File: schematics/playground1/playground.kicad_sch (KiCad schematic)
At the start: 65 parts, among them J1 Conn_01x05, J2 Conn_02x03_Odd_Even, J3 Conn_01x03, J4 Conn_02x04_Odd_Even, SW1 SW_SPST, SW2 SW_Push, SW3 SW_Push, U1 ADS1299, U2 MCP1700x-330xxTT, U3 PIC32MX250F128B_I_SS, U5 LM2931AZ-5.0_TO92, Y1 8MHz

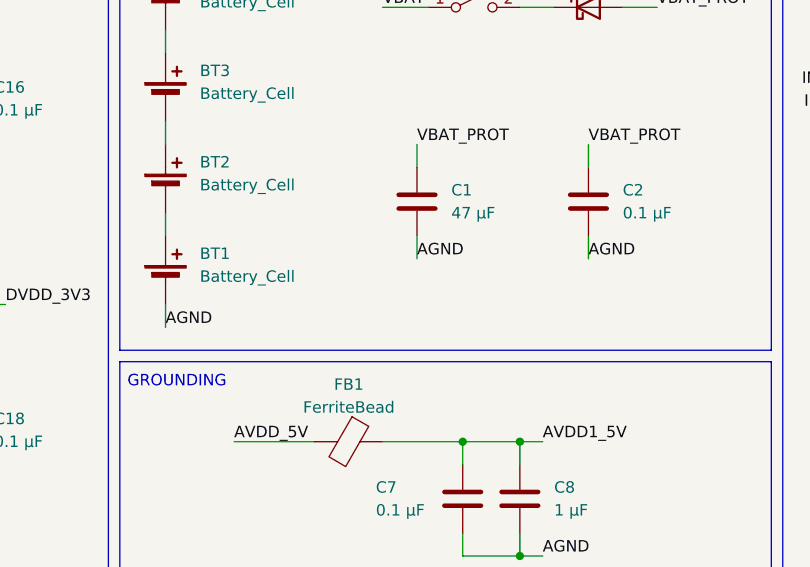
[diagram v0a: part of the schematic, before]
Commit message: change power subsystem to be dgnd, generate gerbers
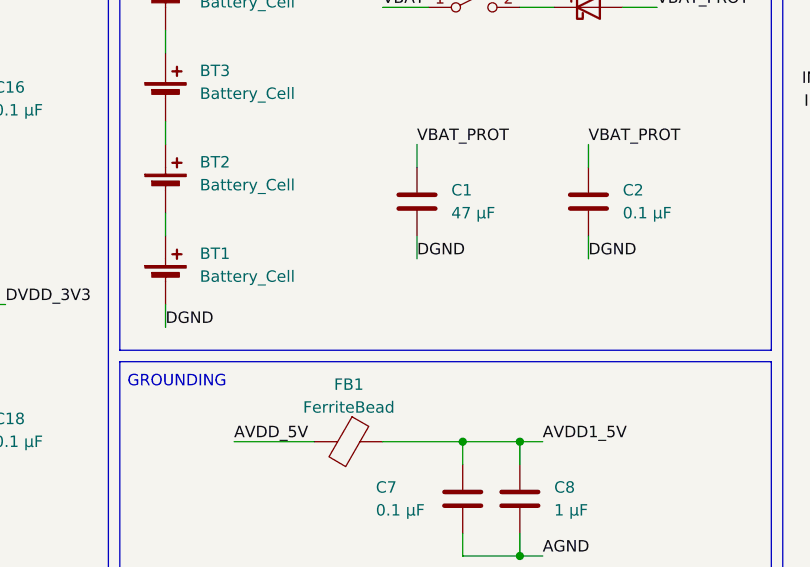
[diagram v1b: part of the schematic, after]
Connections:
- net AGND: no longer BT1.2 (-), C1.2, C2.2
- net DGND: now also BT1.2 (-), C1.2, C2.2
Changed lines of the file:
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@@
 		)
 	)
-	(label "AGND"
+	(label "DGND"
 		(at 196.85 91.44 0)
 		(effects
@@
 		)
 	)
-	(label "AGND"
+	(label "DGND"
 		(at 224.79 83.82 0)
 		(effects
@@
 		)
 	)
-	(label "AGND"
+	(label "DGND"
 		(at 243.84 83.82 0)
 		(effects

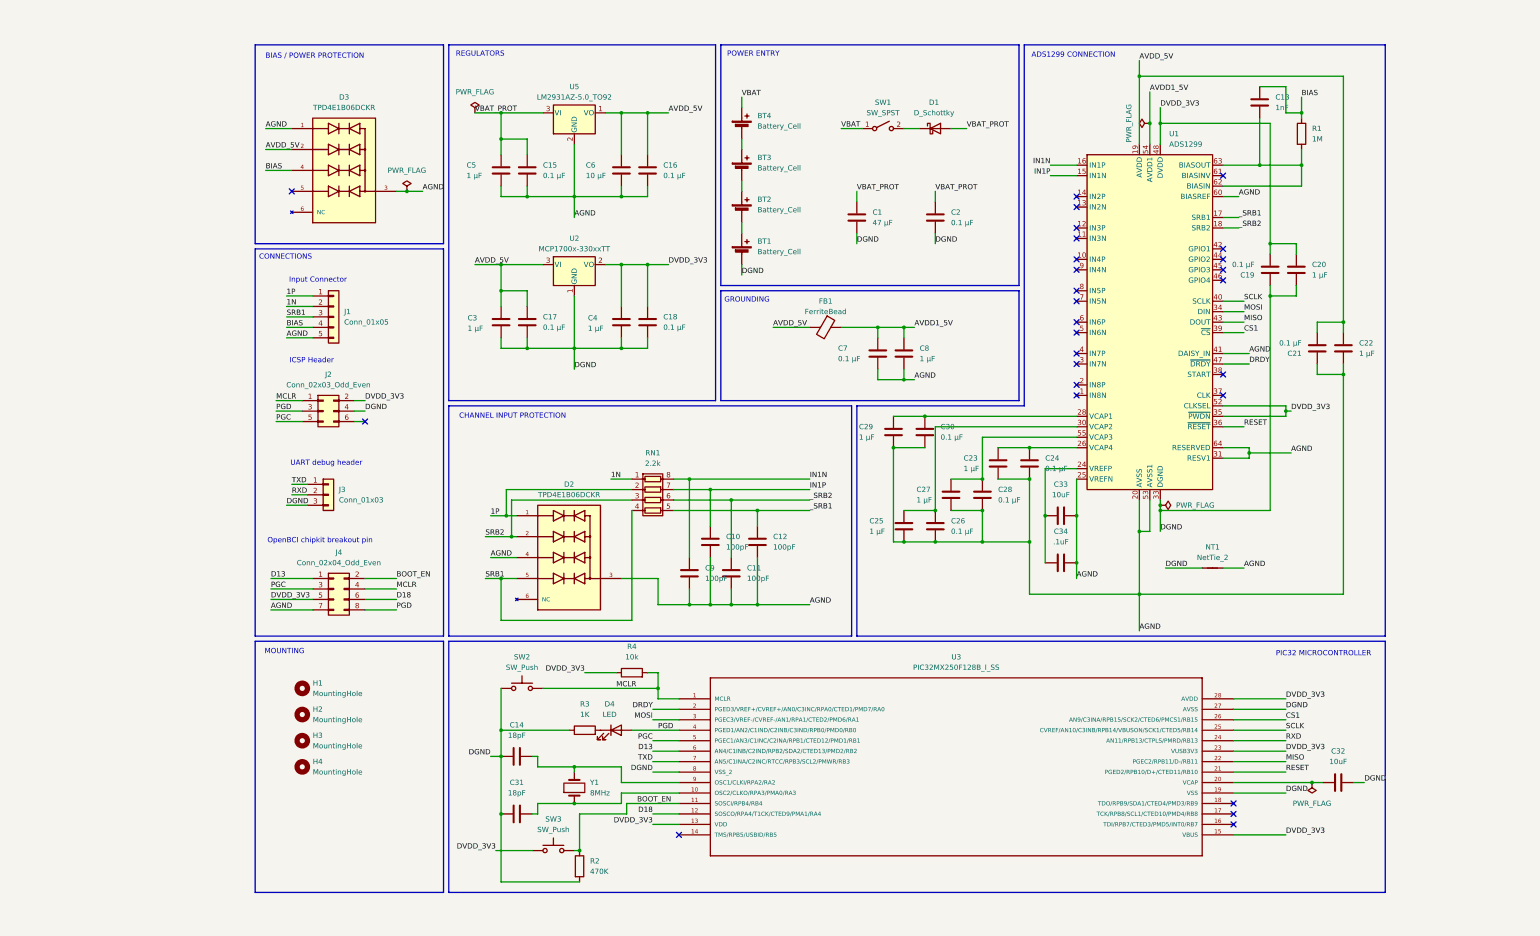
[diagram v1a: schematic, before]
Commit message: add bluetooth chip to schematic and pcb
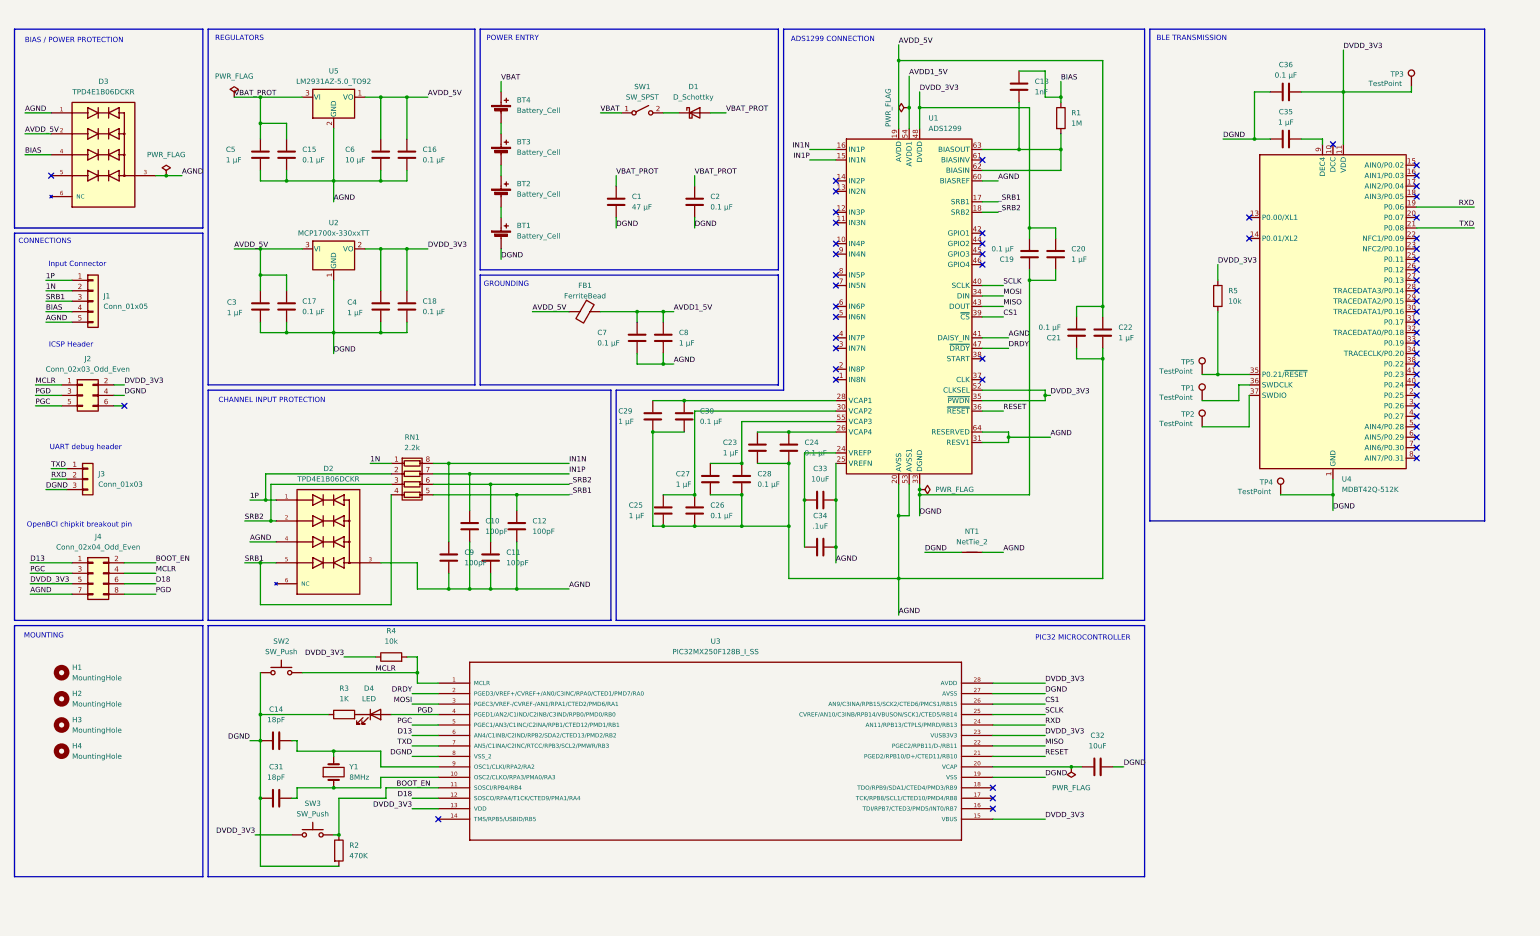
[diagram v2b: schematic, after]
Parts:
- added C35: 1 µF, Capacitor_SMD:C_0603_1608Metric, symbol ble_symbols:C
- added C36: 0.1 µF, Capacitor_SMD:C_0603_1608Metric, symbol ble_symbols:C
- added R5: 10k, Resistor_SMD:R_0603_1608Metric, symbol ble_symbols:R
- added TP1, TP2, TP3, TP4, TP5: TestPoint, TestPoint:TestPoint_Pad_D1.0mm, symbol ble_symbols:TestPoint
- added U4: MDBT42Q-512K, RF_Module:Raytac_MDBT42Q, symbol ble_symbols:MDBT42Q-512K
- BT1, BT2, BT3, BT4: symbol Device:Battery_Cell -> ble_symbols:Battery_Cell
- C1, C10, C11, C12, C13, C14, C15, C16, C17, C18, C19, C2, C20, C21, C22, C23, C24, C25, C26, C27, C28, C29, C3, C30, C31, C32, C33, C34, C4, C5, C6, C7, C8, C9: symbol Device:C -> ble_symbols:C
- D1: symbol Device:D_Schottky -> ble_symbols:D_Schottky
- D2, D3: symbol TPD4E1B06DCKR:TPD4E1B06DCKR -> ble_symbols:TPD4E1B06DCKR
- D4: symbol Device:LED -> ble_symbols:LED
- FB1: symbol Device:FerriteBead -> ble_symbols:FerriteBead
- H1, H2, H3, H4: symbol Mechanical:MountingHole -> ble_symbols:MountingHole
- J1: symbol Connector_Generic:Conn_01x05 -> ble_symbols:Conn_01x05
- J2: symbol Connector_Generic:Conn_02x03_Odd_Even -> ble_symbols:Conn_02x03_Odd_Even
- J3: symbol Connector_Generic:Conn_01x03 -> ble_symbols:Conn_01x03
- J4: symbol Connector_Generic:Conn_02x04_Odd_Even -> ble_symbols:Conn_02x04_Odd_Even
- NT1: symbol Device:NetTie_2 -> ble_symbols:NetTie_2
- R1, R2, R3, R4: symbol Device:R -> ble_symbols:R
- RN1: symbol Device:R_Pack04 -> ble_symbols:R_Pack04
- SW1: symbol Switch:SW_SPST -> ble_symbols:SW_SPST
- SW2, SW3: symbol Switch:SW_Push -> ble_symbols:SW_Push
- U1: symbol Analog_ADC:ADS1299 -> ble_symbols:ADS1299
- U2: symbol Regulator_Linear:MCP1700x-330xxTT -> ble_symbols:MCP1700x-330xxTT
- U3: symbol PIC32MX250F128B_I_SS:PIC32MX250F128B_I_SS -> ble_symbols:PIC32MX250F128B_I_SS
- U5: symbol Regulator_Linear:LM2931AZ-5.0_TO92 -> ble_symbols:LM2931AZ-5.0_TO92
- Y1: symbol Device:Crystal -> ble_symbols:Crystal
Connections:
- net DGND: now also C35.1, C36.1, TP4.1, U4.1 (GND), U4.12 (GND), U4.24 (GND), U4.39 (GND)
- net DVDD_3V3: now also C36.2, R5.1, TP3.1, U4.11 (VDD)
- net RXD: now also U4.19 (P0.06)
- net TXD: now also U4.21 (P0.08)
- new net: R5.2, TP5.1, U4.35 (P0.21/~{RESET})
- new net: TP1.1, U4.36 (SWDCLK)
- new net: TP2.1, U4.37 (SWDIO)
- new net: C35.2, U4.9 (DEC4)
- no-connect marks 27 -> 57
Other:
- note added: "BLE TRANSMISSION"
- moved on the sheet: BT1, BT2, BT3, BT4, C1, C10, C11, C12, C13, C14, C15, C16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

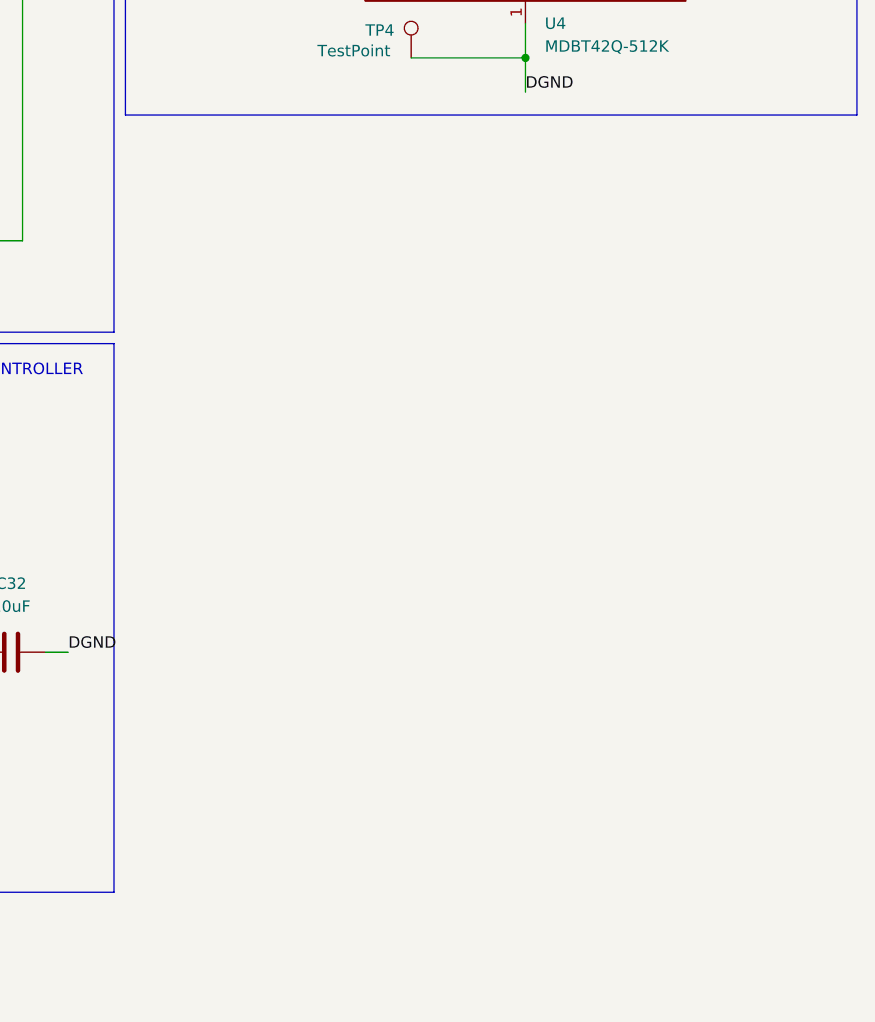
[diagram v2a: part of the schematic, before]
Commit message: audio subsystem added in schematic + footprints
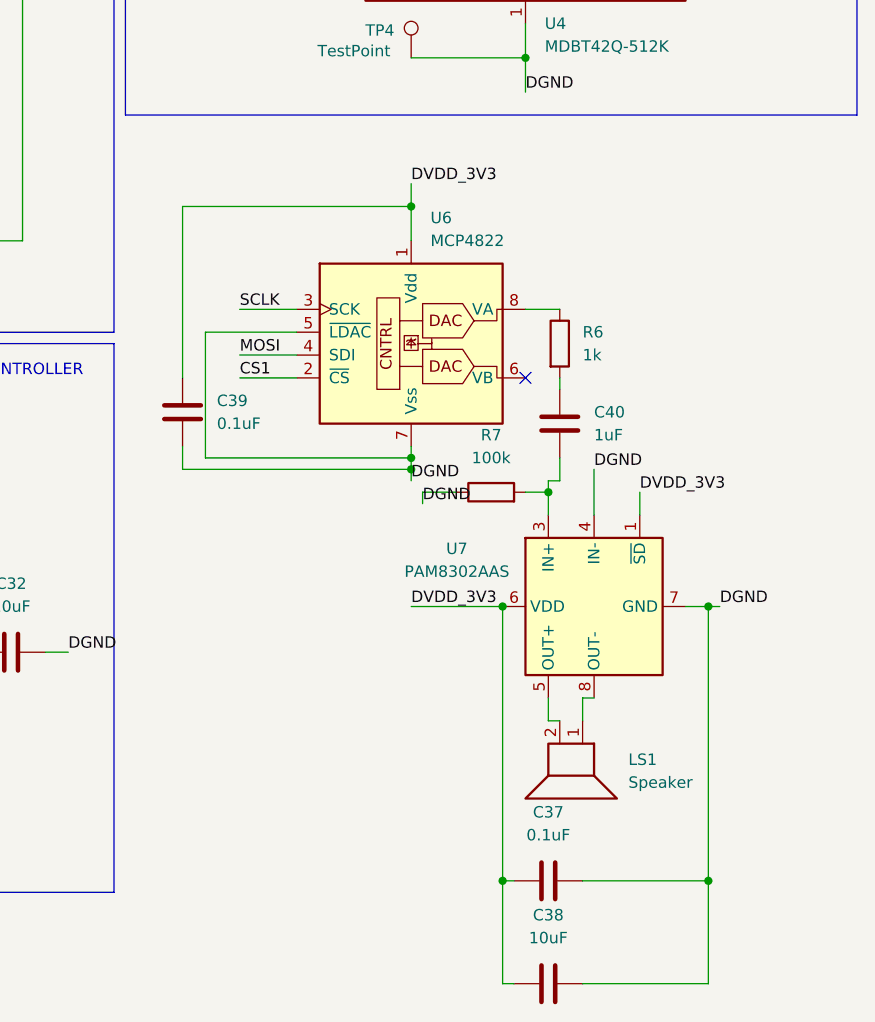
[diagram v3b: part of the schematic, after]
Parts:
- added C37, C39: 0.1uF, Capacitor_SMD:C_0603_1608Metric, symbol Device:C
- added C38: 10uF, Capacitor_SMD:C_0805_2012Metric, symbol Device:C
- added C40: 1uF, Capacitor_SMD:C_0603_1608Metric, symbol Device:C
- added LS1: Speaker, Connector_PinHeader_2.54mm:PinHeader_1x02_P2.54mm_Vertical, symbol Device:Speaker
- added R6: 1k, Resistor_SMD:R_0603_1608Metric, symbol Device:R
- added R7: 100k, Resistor_SMD:R_0603_1608Metric, symbol Device:R
- added U6: MCP4822, Package_SO:MSOP-8_3x3mm_P0.65mm, symbol Analog_DAC:MCP4822
- added U7: PAM8302AAS, Package_SO:MSOP-8_3x3mm_P0.65mm, symbol Amplifier_Audio:PAM8302AAS
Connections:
- net CS1: now also U6.2 (~{CS})
- net DGND: now also C37.2, C38.2, C39.2, R7.1, U6.5 (~{LDAC}), U6.7 (Vss), U7.4 (IN-), U7.7 (GND)
- net DVDD_3V3: now also C37.1, C38.1, C39.1, U6.1 (Vdd), U7.1 (~{SD}), U7.6 (VDD)
- net MOSI: now also U6.4 (SDI)
- net SCLK: now also U6.3 (SCK)
- new net: R6.1, U6.8 (VA)
- new net: C40.1, R6.2
- new net: C40.2, R7.2, U7.3 (IN+)
- new net: LS1.1, U7.8 (OUT-)
- new net: LS1.2, U7.5 (OUT+)
- no-connect marks 57 -> 58

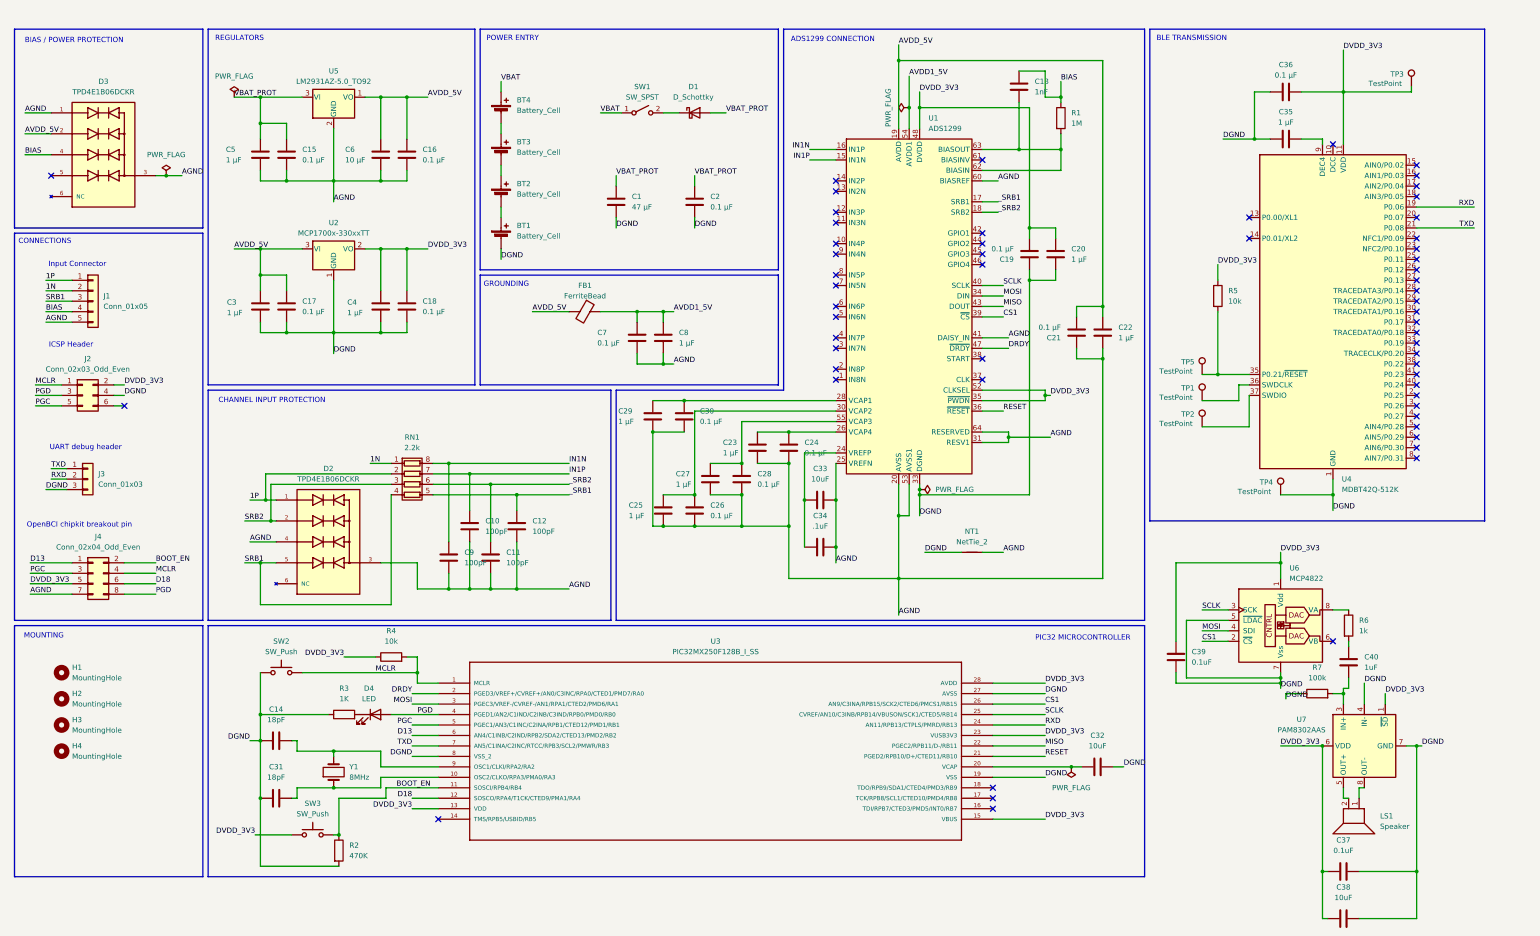
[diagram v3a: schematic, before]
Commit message: clean up audio schematic, wire audio in and move ble
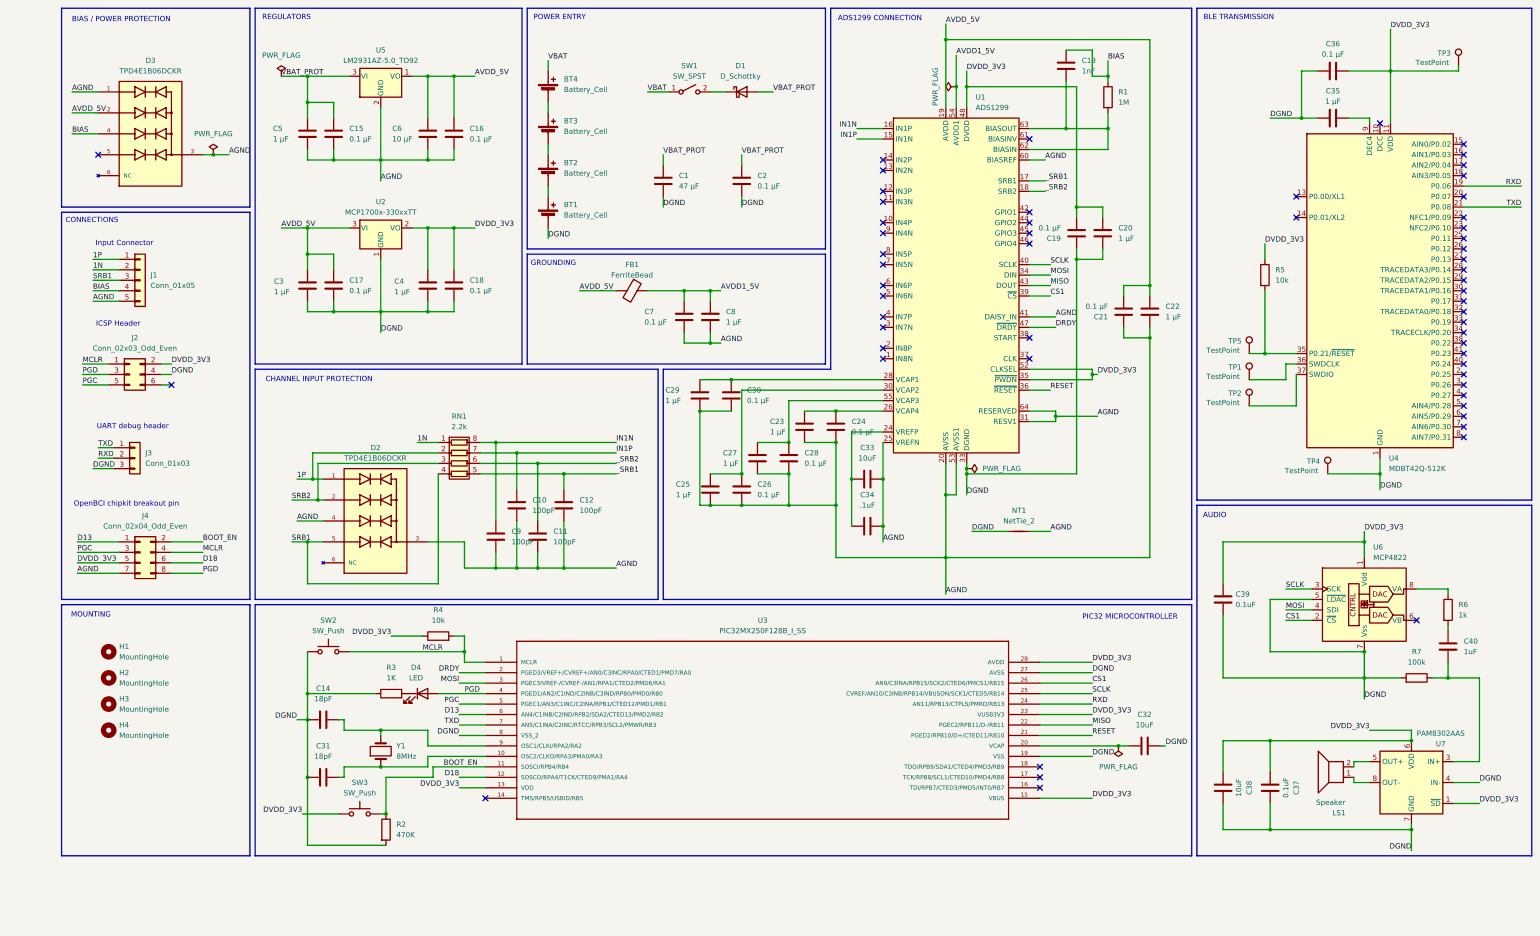
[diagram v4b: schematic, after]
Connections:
- net DGND: now also R7.2; no longer R7.1
- net at C40.2, U7.3 (IN+): now also R7.1; no longer R7.2
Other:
- note added: "AUDIO"
- moved on the sheet: BT1, BT2, BT3, BT4, C1, C10, C11, C12, C13, C14, C15, C16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
